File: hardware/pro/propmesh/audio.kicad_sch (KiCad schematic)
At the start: 0 parts

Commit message: Sheet 04 (audio + SD) captured: mono amp, PCM5102A line-out, microSD
- MAX98357A config resolved datasheet-exact: GAIN_SLOT->GND = 12 dB
  (zero parts); SD_MODE mono mix via 620k to +3V3 (RLARGE formula,
  window computed vs trip points; rail chosen for noise margin and
  the one-rail strap convention). Genuine ADI $0.88@100 dissolved
  the clone question.
- Line-out dropped then REVERSED same day (Colin): PCM5102A second
  DAC on the shared I2S bus, TI Fig.33 literal (SCK grounded = BCK
  PLL), 470R+2.2nF outputs, PJ-320A jack. ~$1.65 for the honest
  version; audio block $3.28@100 verified vs $2.65 estimate.
- PJ-320A mapping settled by geometry after THREE numbering schemes
  collided (datasheet contacts 1-4, import pads 2-5, unnumbered PCB
  layout): L=4 (deepest spring = tip, Colin's argument), R=3,
  GND=2+5. Meter-confirm at bring-up. Import-lie #5 documented.
- microSD TF-01A with D3 pull-up ADDED beyond the pinmap note
  (ESP-IDF: D3 low drops the card into SPI mode); card-detect to a
  test pad.
- Library: pin types set on all four audio imports (amp NC pins
  typed no_connect); peg-hole NPTH fixes on TF-01A and PJ-320A.
- checknet renderer: rail-only parts (pure decoupling) now render in
  their own diagram section — ten invisible caps taught us the
  drawing guide could silently drop parts.
- All four drawn sheets: checknet green, ERC clean.

Co-Authored-By: Claude Fable 5 <noreply@anthropic.com>
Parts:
- added C18, C19: 100p, Capacitor_SMD:C_0603_1608Metric, symbol Device:C
- added C20, C21: 2.2u, Capacitor_SMD:C_0603_1608Metric, symbol Device:C
- added C22, C_A1, C_AV1, C_CPV1, C_DV1, C_SD1: 10u, Capacitor_SMD:C_0805_2012Metric, symbol Device:C
- added C23, C_A2, C_AV2, C_CPV2, C_DV2, C_SD2: 100n, Capacitor_SMD:C_0603_1608Metric, symbol Device:C
- added C24, C25: 2.2n, Capacitor_SMD:C_0603_1608Metric, symbol Device:C
- added CN1: LINE_OUT, propmesh:AUDIO-TH_XKB_PJ-320A, symbol propmesh:PJ-320A
- added Card1: TF-01A, propmesh:TF-SMD_TF-01A, symbol propmesh:TF-01A
- added FB1, FB2: BLM21PG221SN1D, Inductor_SMD:L_0805_2012Metric, symbol Device:FerriteBead
- added J5: SPEAKER, propmesh:CONN-TH_DG381S-3.5-02P-14-00A-H, symbol Connector:Screw_Terminal_01x02
- added R22: 620K, Resistor_SMD:R_0603_1608Metric, symbol Device:R
- added R23, R26, R27, R28: 10k, Resistor_SMD:R_0603_1608Metric, symbol Device:R
- added R24, R25: 470, Resistor_SMD:R_0603_1608Metric, symbol Device:R
- added TP2: TP_CD, TestPoint:TestPoint_Pad_1.5x1.5mm, symbol Connector:TestPoint
- added U7: MAX98357AETE+T, propmesh:TQFN-16_L3.0-W3.0-P0.50-BL-EP1.5, symbol propmesh:MAX98357AETE+T
- added U8: PCM5102APWR, propmesh:TSSOP-20_L6.5-W4.4-P0.65-LS6.4-BL, symbol propmesh:PCM5102APWR
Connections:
- new net: R23.2, U8.17 (XSMT)
- new net: C20.1, U8.2 (CAPP)
- new net: C20.2, U8.4 (CAPM)
- new net: C21.1, U8.5 (VNEG)
- new net: R24.1, U8.6 (OUTL)
- new net: R25.1, U8.7 (OUTR)
- new net: FB1.1, U7.9 (OUTP)
- new net: FB2.1, U7.10 (OUTN)
- new net: Card1.9 (CD), TP2.1
- new net +3V3: C_AV1.1, C_AV2.1, C_CPV1.1, C_CPV2.1, C_DV1.1, C_DV2.1, C_SD1.1, C_SD2.1, Card1.4 (VDD), R22.1, R23.1, R26.1, R27.1, R28.1, U8.1 (CPVDD), U8.20 (DVDD), U8.8 (AVDD)
- new net +5V: C_A1.1, C_A2.1, U7.7 (VDD), U7.8 (VDD)
- new net GND: C18.2, C19.2, C21.2, C22.2, C23.2, C24.2, C25.2, CN1.2, CN1.5, C_A1.2, C_A2.2, C_AV1.2, C_AV2.2, C_CPV1.2, C_CPV2.2, C_DV1.2, C_DV2.2, C_SD1.2, C_SD2.2, Card1.10 (GND), Card1.11 (GND), Card1.12 (GND), Card1.13 (GND), Card1.6 (VSS), U7.11 (GND), U7.15 (GND), U7.17 (EP), U7.2 (GAIN_SLOT), U7.3 (GND), U8.10 (DEMP), U8.11 (FLT), U8.12 (SCK), U8.16 (FMT), U8.19 (DGND), U8.3 (CPGND), U8.9 (AGND)
- new net I2S_BCLK: U7.16 (BCLK), U8.13 (BCK)
- new net I2S_DOUT: U7.1 (DIN), U8.14 (DIN)
- new net I2S_LRCLK: U7.14 (LRCLK), U8.15 (LRCK)
- new net LDO_N: C22.1, C23.1, U8.18 (LDOO)
- new net LINE_L: C24.1, CN1.4, R24.2
- new net LINE_R: C25.1, CN1.3, R25.2
- new net SDM: R22.2, U7.4 (~{SD_MODE})
- new net SD_CLK: Card1.5 (CLK(SCLK))
- new net SD_CMD: Card1.3 (CMD(DI)), R26.2
- new net SD_D0: Card1.7 (DAT0(D0)), R28.2
- new net SD_D3: Card1.2 (CDDAT3(CS)), R27.2
- new net SPK_N: C19.1, FB2.2, J5.2 (Pin_2)
- new net SPK_P: C18.1, FB1.2, J5.1 (Pin_1)
- no-connect marks 0 -> 6
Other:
- note added: "Audio Circuit"
- note added: "Connectors"
- note added: "Line Out DAC"
- note added: "SD Card Holder"

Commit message: Pro schematic complete; enclosure, layout guide, timeline and radio decisions
Schematic: all seven design sheets drawn and green; project-wide ERC at
zero. IR receiver dropped (hidden board can't see a remote — plug-in on
a DIGITAL_IN); GPIO 3 became LED_STRIP_1_CLK; both strip outputs 3- or
4-wire through one octal SN74AHCT541DWR (three revisions of the shifter
in one day, no mode jumpers). Input FET symbol replaced: KiCad 10's
Device:Q_PMOS numbers pins D/G/S and matches no pad — the part would
have been unconnected with no ERC/DRC complaint. All 196 references
renumbered to standard sequential designators (yaml keeps spec names;
the checker prints both). Sheet 08 (test points) and the sheet 01
staged-power link headers specified per spec §2.6 — sheet 01's checker
is red until they are drawn.

checknet.py: symbol pins ⊆ footprint pads check (the silent killer),
multi-unit pin keys + per-unit diagrams (`units:`), symbol-vote sheet
anchoring for half-drawn sheets, orientation-aware net voting, foreign
part reporting, cross-sheet extras no longer crash the report.

Docs: hardware/pro/layout.md — placement by designator, IPC-2221 trace
widths, thermal, silk, ⚠ list, KiCad primer; every chip's datasheet
layout section read (WROOM-1U has NO keep-out; DRV8871 wants a bottom
GND pour; MAX98357A output-trace numbers). Enclosure plan (spec §2.3):
Multilink RNI-1500 / RNI-300, DRiBOX Medium, Joinfworld clear-lid box,
icotek KEL-DPZ entry plate, fit rule 210×140×60 mm inside; PSU
defaults (§2.9) and the 10 A input-path note. Software plan: timeline
design (ramps native, live scrub v1, Cue.start_offset_ms in schema),
yard access (walk-up AP, WireGuard-in-firmware, BYO remote), WiFi-PHY
radio decision vs Zigbee/BLE/LoRa, console served-from-bridge budget,
USB stays in CDC/JTAG mode (no auto-program transistors needed).

Co-Authored-By: Claude Fable 5.1 <noreply@anthropic.com>
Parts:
- renumbered C20 to C24, C22 to C25, C23 to C26, C21 to C27, C_A1 to C28, C_A2 to C29, C18 to C30, C19 to C31, C24 to C32, C25 to C33, C_DV1 to C34, C_DV2 to C35, C_AV1 to C36, C_AV2 to C37, C_CPV1 to C38, C_CPV2 to C39, C_SD1 to C40, C_SD2 to C41, J5 to J35, R22 to R27, R23 to R28, R24 to R29, R25 to R30, R27 to R31, R28 to R32, R26 to R33, U8 to U10, U7 to U9

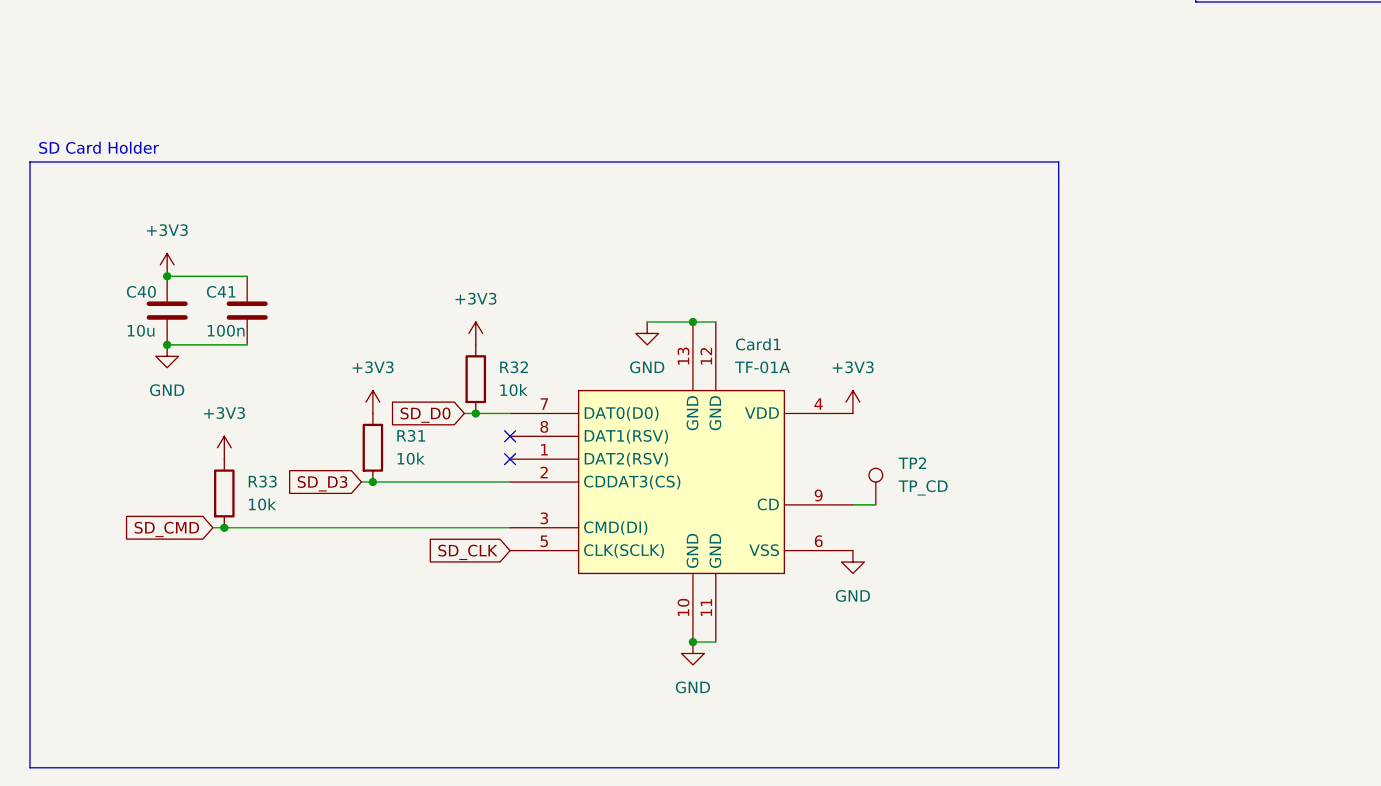
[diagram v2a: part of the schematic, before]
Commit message: Pro v0.1 schematic complete; board cleanup pass, parity 0
Schematic: all datasheet-review changes drawn (decisions 1A, 2A, 3B,
OE on GPIO 37, 4B). All eight sheet checkers ALL NETS MATCH, ERC 0
errors / 0 warnings, pinmap matches generated headers.
- sheet 03: second PCA9685 (U12, 0x41) with B-straps, PCA_OE net with
  10k pull-up (R59); DC FETs Q1-Q6 = SI2356DS
- sheets 02/04/05/07/08: USB link/22R/VBUS cap, SD DAT1/DAT2 pull-ups,
  shifter pulldowns, 2.2k 1206 sensor Rs; R53 (GPIO3 pulldown) now drawn
  on sheet 05, specs moved to match

Board (KiCad closed, backup kept):
- F8 done, schematic parity 0; orphan DNP R53 removed
- mounting holes H1-H4, board-only, excluded from BOM/position files
- minimum drill 0.3 -> 0.2 mm: U2's own 0.2/0.6 thermal vias; JLCPCB
  4-layer standard cost for 0.2 mm holes with >= 0.45 mm pads
- DG128-02P pads 2.3 -> 2.8 mm (J17 10 A input; library edited too)
- DRV8871 exposed-pad paste inset 0.1 mm (library edited too)
- 43 parts snapped to grid; snapgrid.py now exempts J20/J22 so the
  StepStick rows stay 12.70 mm
- DRC: 11 courtyard overlaps left (3 accepted terminal gangs, 8 in the
  sensor corner from the 1206 resistors) + silkscreen

Tools: checknet.py net vote ignores orientation for R/C/L (three
upside-down pull-ups had out-voted the chip pin on sheet 04); verified
it still catches a shorted net and a mis-wired pull-up.
checksetup.py: min drill 0.2.

Also includes the Mini module selection and KiCad project started in
another session (2026-09-19).

Co-Authored-By: Claude Opus 5.5 <noreply@anthropic.com>
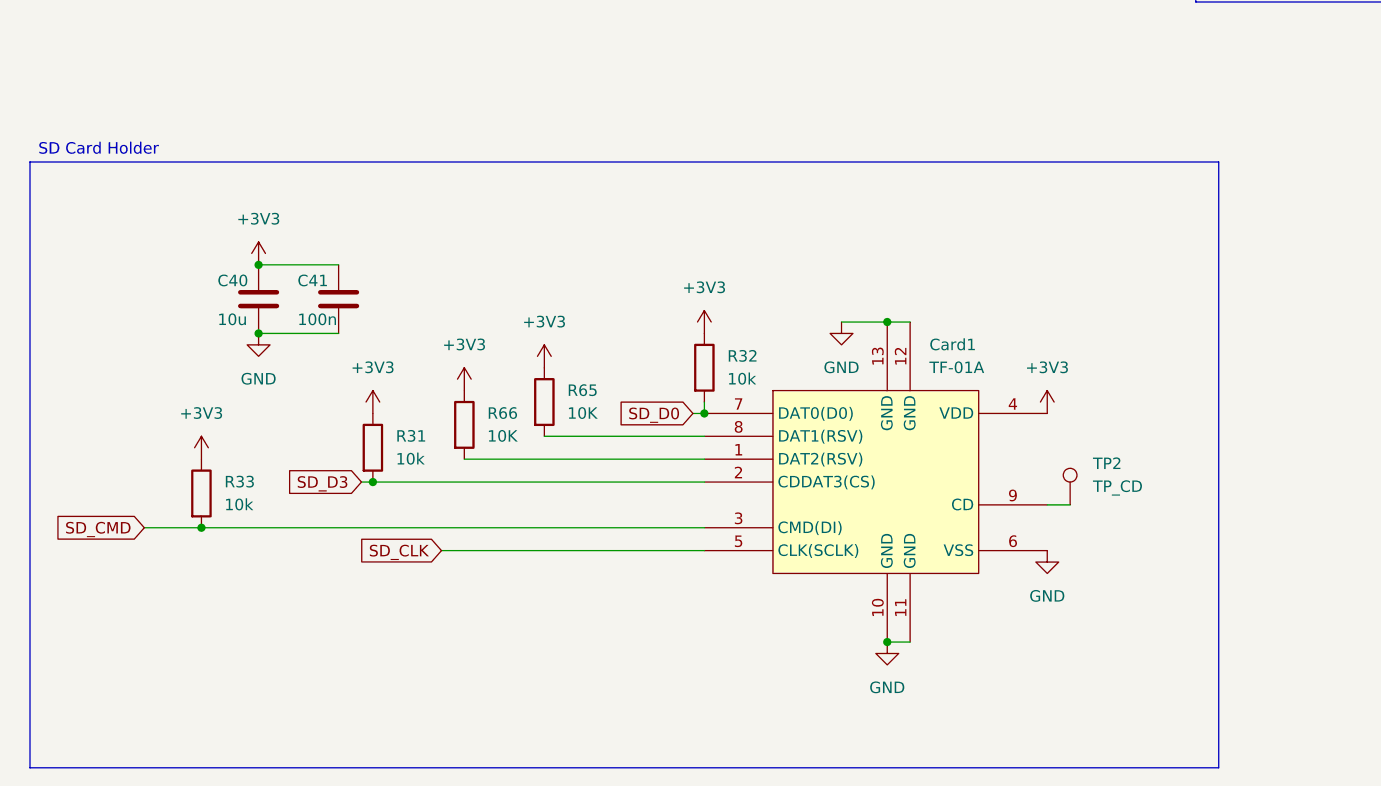
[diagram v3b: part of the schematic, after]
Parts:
- added R65, R66: 10K, Resistor_SMD:R_0603_1608Metric, symbol Device:R
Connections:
- net +3V3: now also R65.1, R66.1
- net at Card1.1 (DAT2(RSV)): now also R66.2
- net at Card1.8 (DAT1(RSV)): now also R65.2
- no-connect marks 6 -> 4
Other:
- moved on the sheet: C40, C41, Card1, R32, R33, TP2
